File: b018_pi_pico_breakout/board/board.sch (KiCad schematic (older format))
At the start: 8 parts, among them J1 SPI_2x3, J2 I2C_2x2, J3 UART_2x2, J4 SPI_2x3, J5 I2C_2x2, J6 UART_2x2, J7 ADC_2x3, U1 Pico

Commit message: added slave UART, new connectors and a debug port
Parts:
- added FB1: Ferrite_Bead_Small, Inductor_SMD:L_0805_2012Metric, symbol Device:Ferrite_Bead_Small
- added J8: DebugEdge_02x05, on_edge:on_edge_2x05_device, symbol put_on_edge:DebugEdge_02x05
- added R1, R2, R3, R4, R5, R6: 10k, Resistor_SMD:R_0603_1608Metric, symbol Device:R_Small
- J1: footprint on_edge:on_edge_2x05_host -> on_edge:on_edge_2x05_up_host; symbol board-rescue:SPI_2x3-put_on_edge -> put_on_edge:002_SPI
- J2: footprint on_edge:on_edge_2x05_host -> on_edge:on_edge_2x05_up_host; symbol board-rescue:I2C_2x2-put_on_edge -> put_on_edge:001_I2C
- J3: footprint on_edge:on_edge_2x05_host -> on_edge:on_edge_2x05_device; symbol board-rescue:UART_2x2-put_on_edge -> put_on_edge:010_UART
- J4: symbol board-rescue:SPI_2x3-put_on_edge -> put_on_edge:002_SPI
- J5: symbol board-rescue:I2C_2x2-put_on_edge -> put_on_edge:001_I2C
- J6: symbol board-rescue:UART_2x2-put_on_edge -> put_on_edge:010_UART
- J7: symbol board-rescue:ADC_2x3-put_on_edge -> put_on_edge:007_ADC
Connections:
- net labels added: +5V
- net labels removed: ADC3
- wire segments 71 -> 123
- no-connect marks 2 -> 16

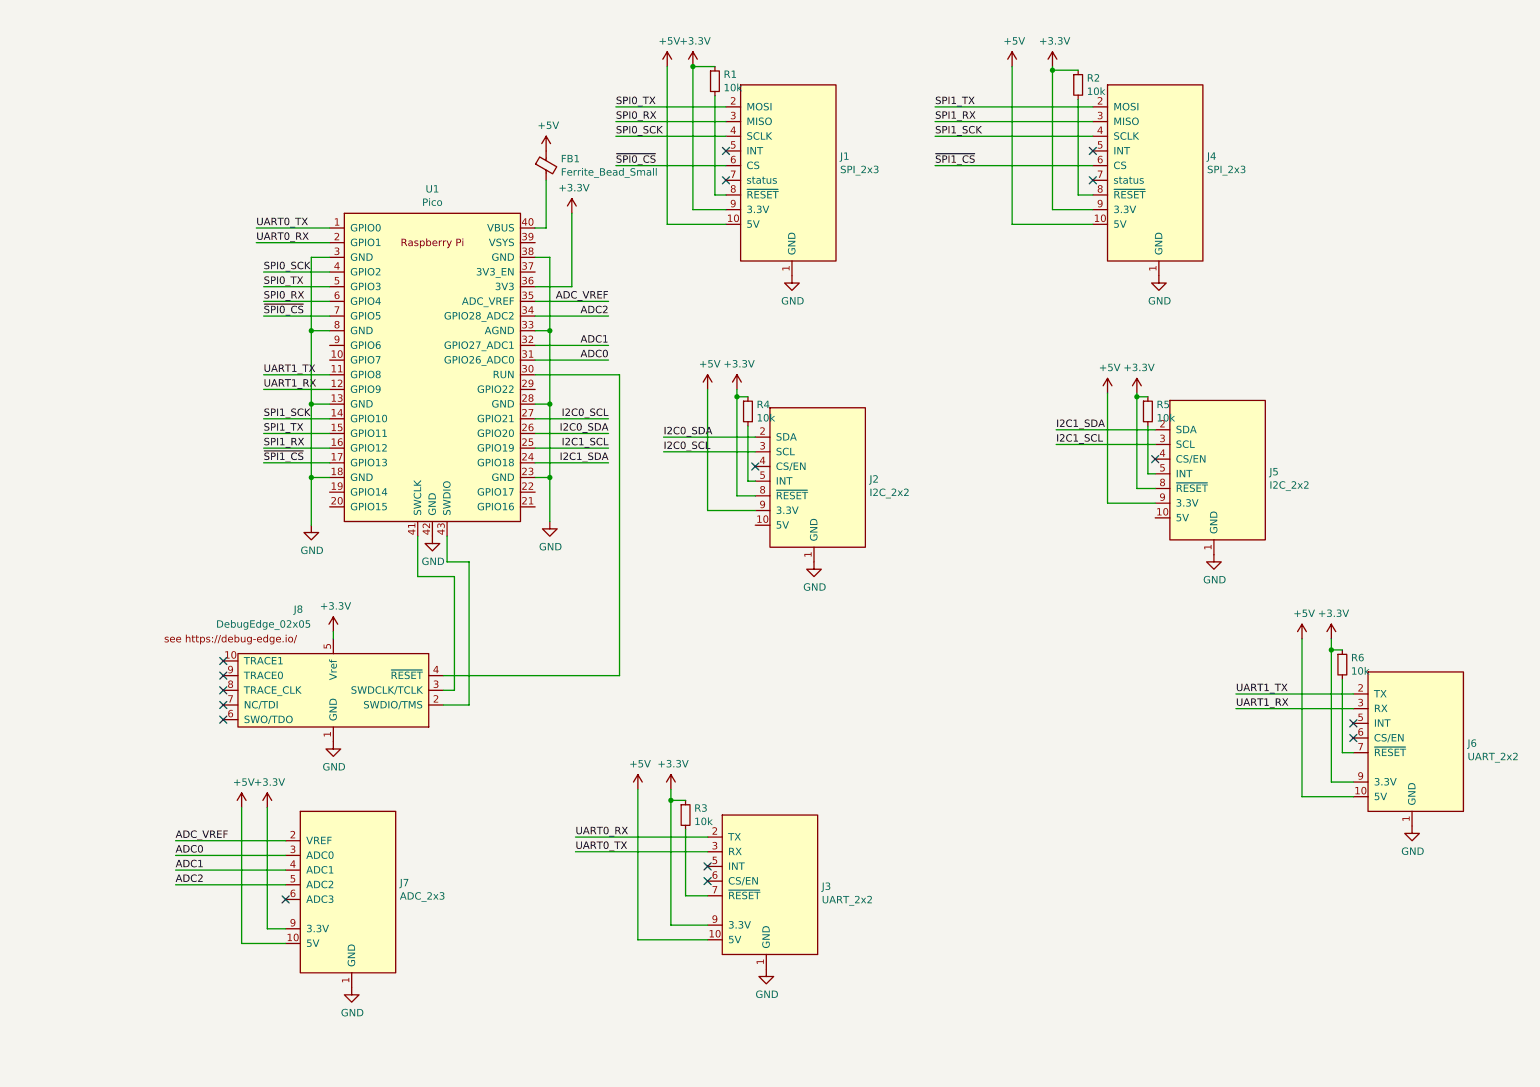
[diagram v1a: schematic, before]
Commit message: updated pico board to use the rp2040
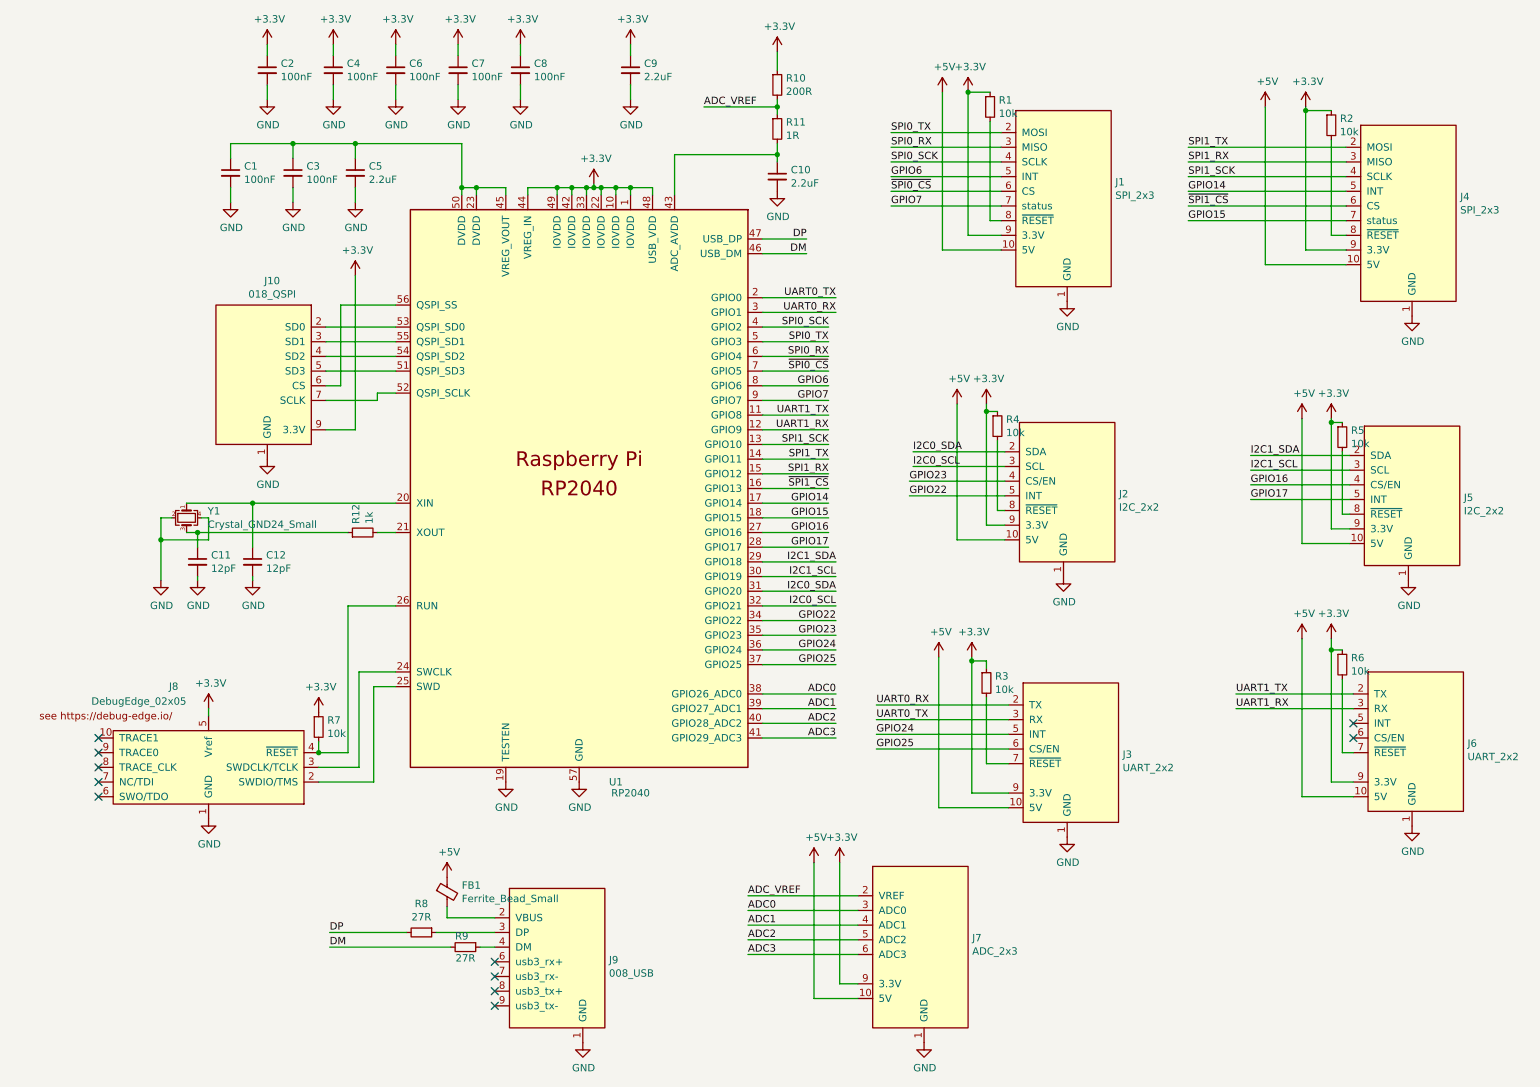
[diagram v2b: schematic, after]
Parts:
- removed U1: Pico, MCU_RaspberryPi_and_Boards:RPi_Pico_SMD_TH, symbol MCU_RaspberryPi_and_Boards:Pico
- added C1, C2, C3, C4, C6, C7, C8: 100nF, Capacitor_SMD:C_0603_1608Metric, symbol Device:C_Small
- added C10, C5, C9: 2.2uF, Capacitor_SMD:C_0603_1608Metric, symbol Device:C_Small
- added C11, C12: 12pF, Capacitor_SMD:C_0603_1608Metric, symbol Device:C_Small
- added J10: 018_QSPI, on_edge:on_edge_2x05_up_host, symbol put_on_edge:018_QSPI
- added J9: 008_USB, on_edge:on_edge_2x05_device, symbol put_on_edge:008_USB
- added R10: 200R, Resistor_SMD:R_0603_1608Metric, symbol Device:R_Small
- added R11: 1R, Resistor_SMD:R_0603_1608Metric, symbol Device:R_Small
- added R12: 1k, Resistor_SMD:R_0603_1608Metric, symbol Device:R_Small
- added R7: 10k, Resistor_SMD:R_0603_1608Metric, symbol Device:R_Small
- added R8, R9: 27R, Resistor_SMD:R_0603_1608Metric, symbol Device:R_Small
- added U1: RP2040, Package_DFN_QFN:QFN-56-1EP_7x7mm_P0.4mm_EP5.6x5.6mm, symbol MCU_RaspberryPi_and_Boards:RP2040
- added Y1: Crystal_GND24_Small, Crystal:Crystal_SMD_Abracon_ABM8G-4Pin_3.2x2.5mm, symbol Device:Crystal_GND24_Small
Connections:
- net +3V3: now also J2.9 (3.3V), J5.9 (3.3V), C2.1, C4.1, C6.1, C7.1, C8.1, C9.1, J10.9 (3.3V), R10.1, R7.1, U1.1 (IOVDD), U1.10 (IOVDD), U1.22 (IOVDD), U1.33 (IOVDD), U1.42 (IOVDD), U1.44 (VREG_IN), U1.48 (USB_VDD), U1.49 (IOVDD); no longer J2.8 (~RESET), J5.8 (~RESET)
- net +5V: now also J2.10 (5V), J5.10 (5V); no longer J2.9 (3.3V), J5.9 (3.3V)
- net ADC0: now also U1.38 (GPIO26_ADC0)
- net ADC1: now also U1.39 (GPIO27_ADC1)
- net ADC2: now also U1.40 (GPIO28_ADC2)
- net ADC_VREF: now also R10.2, R11.1
- net GND: now also C1.2, C10.2, C11.2, C12.2, C2.2, C3.2, C4.2, C5.2, C6.2, C7.2, C8.2, C9.2, J10.1 (GND), J9.1 (GND), U1.19 (TESTEN), U1.57 (GND), Y1.2, Y1.4
- net I2C0_SCL: now also U1.32 (GPIO21)
- net I2C0_SDA: now also U1.31 (GPIO20)
- net I2C1_SCL: now also U1.30 (GPIO19)
- net I2C1_SDA: now also U1.29 (GPIO18)
- net SPI0_RX: now also U1.6 (GPIO4)
- net SPI0_SCK: now also U1.4 (GPIO2)
- net SPI0_TX: now also U1.5 (GPIO3)
- net SPI1_RX: now also U1.15 (GPIO12)
- net SPI1_SCK: now also U1.13 (GPIO10)
- net SPI1_TX: now also U1.14 (GPIO11)
- net UART0_RX: now also U1.3 (GPIO1)
- net UART0_TX: now also U1.2 (GPIO0)
- net UART1_RX: now also U1.12 (GPIO9)
- net UART1_TX: now also U1.11 (GPIO8)
- net ~SPI0_CS: now also U1.7 (GPIO5)
- net ~SPI1_CS: now also U1.16 (GPIO13)
- net at J8.4 (~RESET~): now also R7.2, U1.26 (RUN)
- net at FB1.2: now also J9.2 (VBUS)
- net at J8.3 (SWDCLK/TCLK): now also U1.24 (SWCLK)
- net at J8.2 (SWDIO/TMS): now also U1.25 (SWD)
- net GPIO23: now reaches J2.4 (CS/EN)
- net GPIO23: now also U1.35 (GPIO23)
- net at R4.2: now also J2.8 (~RESET); no longer J2.5 (INT)
- net GPIO16: now reaches J5.4 (CS/EN)
- net GPIO16: now also U1.27 (GPIO16)
- net at R5.2: now also J5.8 (~RESET); no longer J5.5 (INT)
- net GPIO24: now reaches J3.5 (INT)
- net GPIO24: now also U1.36 (GPIO24)
- net GPIO25: now reaches J3.6 (CS/EN)
- net GPIO25: now also U1.37 (GPIO25)
- net GPIO6: now reaches J1.5 (INT)
- net GPIO6: now also U1.8 (GPIO6)
- net GPIO7: now reaches J1.7 (status)
- net GPIO7: now also U1.9 (GPIO7)
- net GPIO14: now reaches J4.5 (INT)
- net GPIO14: now also U1.17 (GPIO14)
- net GPIO15: now reaches J4.7 (status)
- net GPIO15: now also U1.18 (GPIO15)
- net ADC3: now reaches J7.6 (ADC3)
- net ADC3: now also U1.41 (GPIO29_ADC3)
- new net: C12.1, U1.20 (XIN), Y1.1
- new net: R12.2, U1.21 (XOUT)
- new net: C1.1, C3.1, C5.1, U1.23 (DVDD), U1.45 (VREG_VOUT), U1.50 (DVDD)
- new net: C10.1, R11.2, U1.43 (ADC_AVDD)
- new net: J10.5 (SD3), U1.51 (QSPI_SD3)
- new net: J10.7 (SCLK), U1.52 (QSPI_SCLK)
- new net: J10.2 (SD0), U1.53 (QSPI_SD0)
- new net: J10.4 (SD2), U1.54 (QSPI_SD2)
- new net: J10.3 (SD1), U1.55 (QSPI_SD1)
- new net: J10.6 (CS), U1.56 (QSPI_SS)
- new net: J9.3 (DP), R8.1
- new net: J9.4 (DM), R9.1
- new net: C11.1, R12.1, Y1.3
- new net DM: R9.2, U1.46 (USB_DM)
- new net DP: R8.2, U1.47 (USB_DP)
- new net GPIO17: J5.5 (INT), U1.28 (GPIO17)
- new net GPIO22: J2.5 (INT), U1.34 (GPIO22)
- no-connect marks 16 -> 11
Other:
- moved on the sheet: FB1, J1, J2, J3, J4, J5, J7, J8, R1, R2, R3, R4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
